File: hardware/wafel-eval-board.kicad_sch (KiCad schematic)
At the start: 57 parts, among them Q101 AO3422, U101 TPS70933, U102 LM5163DDA

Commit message: fixes
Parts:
- removed H101: BAT+, MountingHole:MountingHole_3.2mm_M3_Pad, symbol Mechanical:MountingHole_Pad
- removed H102: CELL15, MountingHole:MountingHole_3.2mm_M3_Pad, symbol Mechanical:MountingHole_Pad
- removed H103: CELL13, MountingHole:MountingHole_3.2mm_M3_Pad, symbol Mechanical:MountingHole_Pad
- removed H104: CELL11, MountingHole:MountingHole_3.2mm_M3_Pad, symbol Mechanical:MountingHole_Pad
- removed H111: CELL16, MountingHole:MountingHole_3.2mm_M3_Pad, symbol Mechanical:MountingHole_Pad
- removed H112: CELL14, MountingHole:MountingHole_3.2mm_M3_Pad, symbol Mechanical:MountingHole_Pad
- removed H113: CELL12, MountingHole:MountingHole_3.2mm_M3_Pad, symbol Mechanical:MountingHole_Pad
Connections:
- net CELL10: now also F101.1, F102.1
- removed net CELL17: F101.1, F102.1, F103.2
- new net CELL_TOP: F103.2
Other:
- added sheet CB Mosfets (cb-mosfets.kicad_sch)
- sheet Frontend ports: added VC[0..10]; removed CELL[0..17], CH
- sheet MCU ports: added BAT{ADC EN}; removed none
- moved on the sheet: F101, F102, H105, H106, H107, H108, H109, H110, H114, H115, H116, H117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

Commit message: add bat{en adc}
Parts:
- renumbered H105 to H101, H106 to H102, H107 to H103, H108 to H104, H109 to H105, H110 to H106, H114 to H107, H115 to H108, H116 to H109, H117 to H110, H118 to H111, H119 to H112, H120 to H113, H121 to H114
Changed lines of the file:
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@@
 		(in_pos_files yes)
 		(dnp no)
-		(property "Reference" "H109"
+		(property "Reference" "H105"
 			(at 29.21 130.8099 90)
 			(show_name no)
@@
 			(project "wafel-eval-board"
 				(path "/3e668e3e-3e16-4665-a807-4735962c41d3"
-					(reference "H109")
+					(reference "H105")
 					(unit 1)
 				)
@@
 		(in_pos_files yes)
 		(dnp no)
-		(property "Reference" "H116"
+		(property "Reference" "H109"
 			(at 43.18 118.1099 90)
 			(show_name no)
@@
 			(project "wafel-eval-board"
 				(path "/3e668e3e-3e16-4665-a807-4735962c41d3"
-					(reference "H116")
+					(reference "H109")
 					(unit 1)
 				)
@@
 		(in_pos_files yes)
 		(dnp no)
-		(property "Reference" "H106"
+		(property "Reference" "H102"
 			(at 29.21 115.5699 90)
 			(show_name no)
@@
 			(project "wafel-eval-board"
 				(path "/3e668e3e-3e16-4665-a807-4735962c41d3"
-					(reference "H106")
+					(reference "H102")
 					(unit 1)
 				)
@@
 		(in_pos_files yes)
 		(dnp no)
-		(property "Reference" "H115"
+		(property "Reference" "H108"
 			(at 43.18 113.0299 90)
 			(show_name no)
@@
 			(project "wafel-eval-board"
 				(path "/3e668e3e-3e16-4665-a807-4735962c41d3"
-					(reference "H115")
+					(reference "H108")
 					(unit 1)
 				)
@@
 		(in_pos_files yes)
 		(dnp no)
-		(property "Reference" "H108"
+		(property "Reference" "H104"
 			(at 29.21 125.7299 90)
 			(show_name no)
@@
 			(project "wafel-eval-board"
 				(path "/3e668e3e-3e16-4665-a807-4735962c41d3"
-					(reference "H108")
+					(reference "H104")
 					(unit 1)
 				)
@@
 		(in_pos_files yes)
 		(dnp no)
-		(property "Reference" "H105"
+		(property "Reference" "H101"
 			(at 29.21 110.4899 90)
 			(show_name no)
@@
 			(project "wafel-eval-board"
 				(path "/3e668e3e-3e16-4665-a807-4735962c41d3"
-					(reference "H105")
+					(reference "H101")
 					(unit 1)
 				)
@@
 		(in_pos_files yes)
 		(dnp no)
-		(property "Reference" "H120"
+		(property "Reference" "H113"
 			(at 273.05 146.0499 90)
 			(show_name no)
@@
 			(project "wafel-eval-board"
 				(path "/3e668e3e-3e16-4665-a807-4735962c41d3"
-					(reference "H120")
+					(reference "H113")
 					(unit 1)
 				)
@@
 		(in_pos_files yes)
 		(dnp no)
-		(property "Reference" "H121"
+		(property "Reference" "H114"
 			(at 273.05 153.6699 90)
 			(show_name no)
@@
 			(project "wafel-eval-board"
 				(path "/3e668e3e-3e16-4665-a807-4735962c41d3"
-					(reference "H121")
+					(reference "H114")
 					(unit 1)
 				)
@@
 		(in_pos_files yes)
 		(dnp no)
-		(property "Reference" "H110"
+		(property "Reference" "H106"
 			(at 24.13 135.89 90)
 			(show_name no)
@@
 			(project "wafel-eval-board"
 				(path "/3e668e3e-3e16-4665-a807-4735962c41d3"
-					(reference "H110")
+					(reference "H106")
 					(unit 1)
 				)
@@
 		(in_pos_files yes)
 		(dnp no)
-		(property "Reference" "H119"
+		(property "Reference" "H112"
 			(at 43.18 133.3499 90)
 			(show_name no)
@@
 			(project "wafel-eval-board"
 				(path "/3e668e3e-3e16-4665-a807-4735962c41d3"
-					(reference "H119")
+					(reference "H112")
 					(unit 1)
 				)
@@
 		(in_pos_files yes)
 		(dnp no)
-		(property "Reference" "H117"
+		(property "Reference" "H110"
 			(at 43.18 123.1899 90)
 			(show_name no)
@@
 			(project "wafel-eval-board"
 				(path "/3e668e3e-3e16-4665-a807-4735962c41d3"
-					(reference "H117")
+					(reference "H110")
 					(unit 1)
 				)
@@
 		(in_pos_files yes)
 		(dnp no)
-		(property "Reference" "H118"
+		(property "Reference" "H111"
 			(at 43.18 128.2699 90)
 			(show_name no)
@@
 			(project "wafel-eval-board"
 				(path "/3e668e3e-3e16-4665-a807-4735962c41d3"
-					(reference "H118")
+					(reference "H111")
 					(unit 1)
 				)
@@
 		(in_pos_files yes)
 		(dnp no)
-		(property "Reference" "H107"
+		(property "Reference" "H103"
 			(at 29.21 120.6499 90)
 			(show_name no)
@@
 			(project "wafel-eval-board"
 				(path "/3e668e3e-3e16-4665-a807-4735962c41d3"
-					(reference "H107")
+					(reference "H103")
 					(unit 1)
 				)
@@
 		(in_pos_files yes)
 		(dnp no)
-		(property "Reference" "H114"
+		(property "Reference" "H107"
 			(at 43.18 107.9499 90)
 			(show_name no)
@@
 			(project "wafel-eval-board"
 				(path "/3e668e3e-3e16-4665-a807-4735962c41d3"
-					(reference "H114")
+					(reference "H107")
 					(unit 1)
 				)

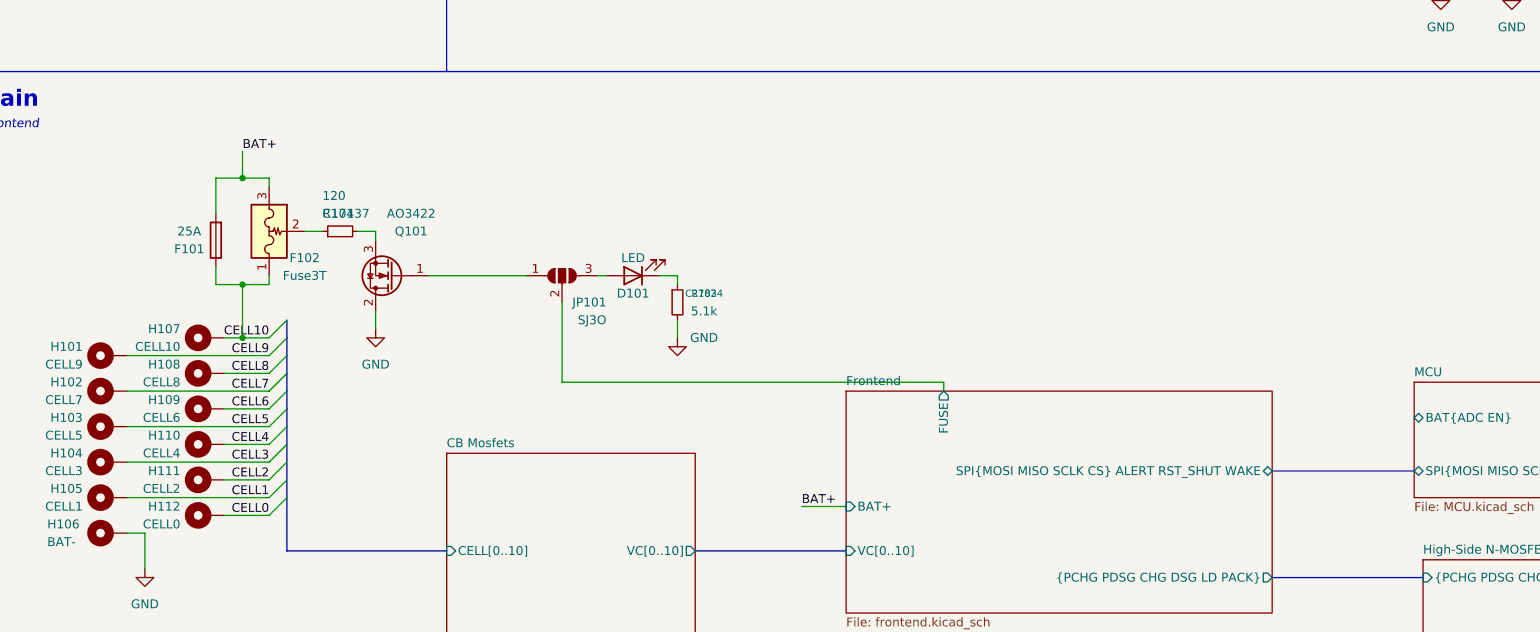
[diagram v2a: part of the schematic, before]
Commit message: simplify page
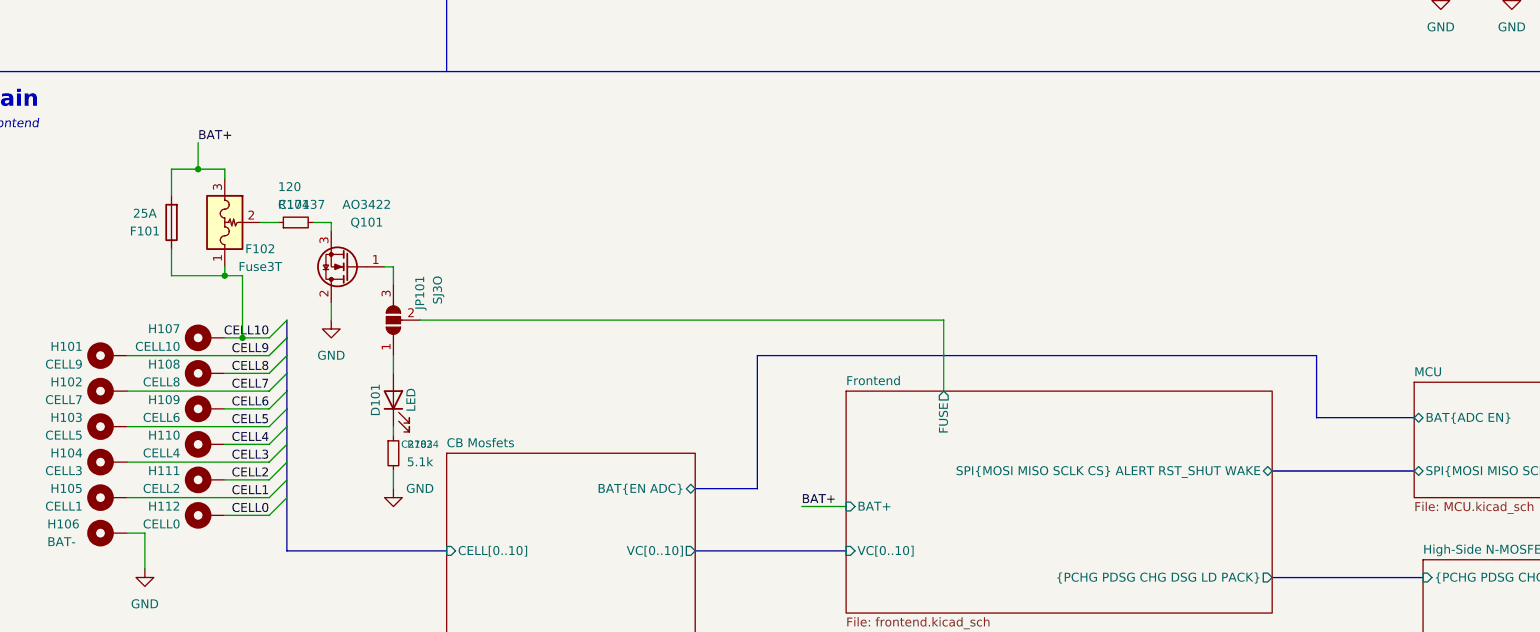
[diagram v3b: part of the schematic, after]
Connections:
- net at D101.2 (A): now also JP101.1 (A); no longer JP101.3 (B)
- net at Q101.1 (G): now also JP101.3 (B); no longer JP101.1 (A)
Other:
- sheet CB Mosfets ports: added BAT{EN ADC}; removed none
- moved on the sheet: D101, F101, F102, JP101, Q101, R101, R102

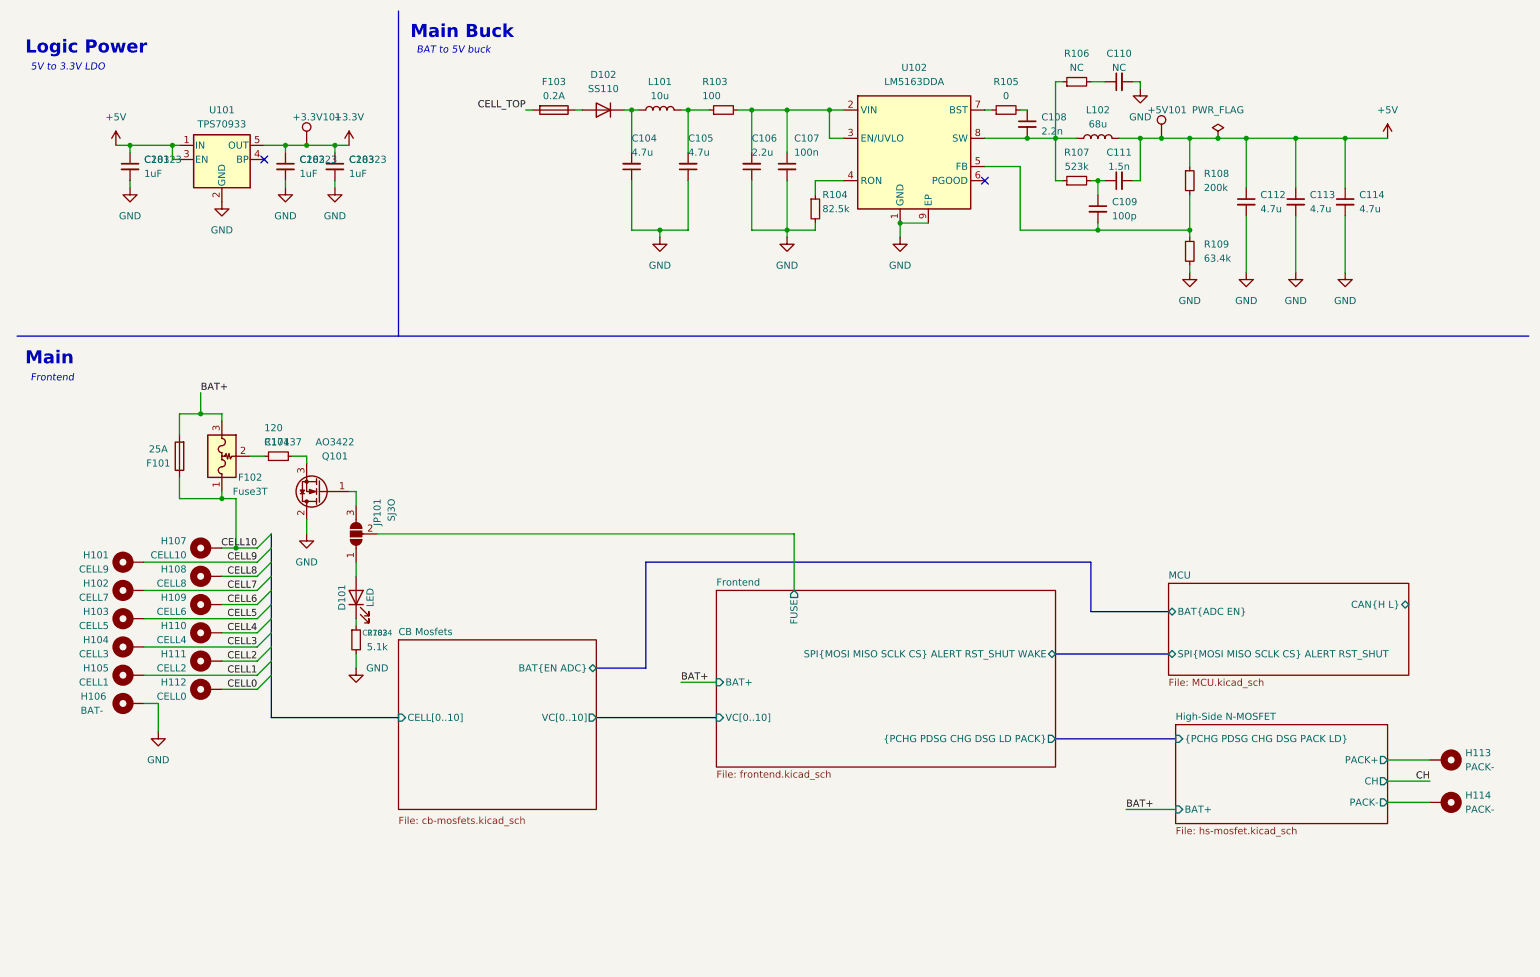
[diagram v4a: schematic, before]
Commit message: switch capasitors to 220mf
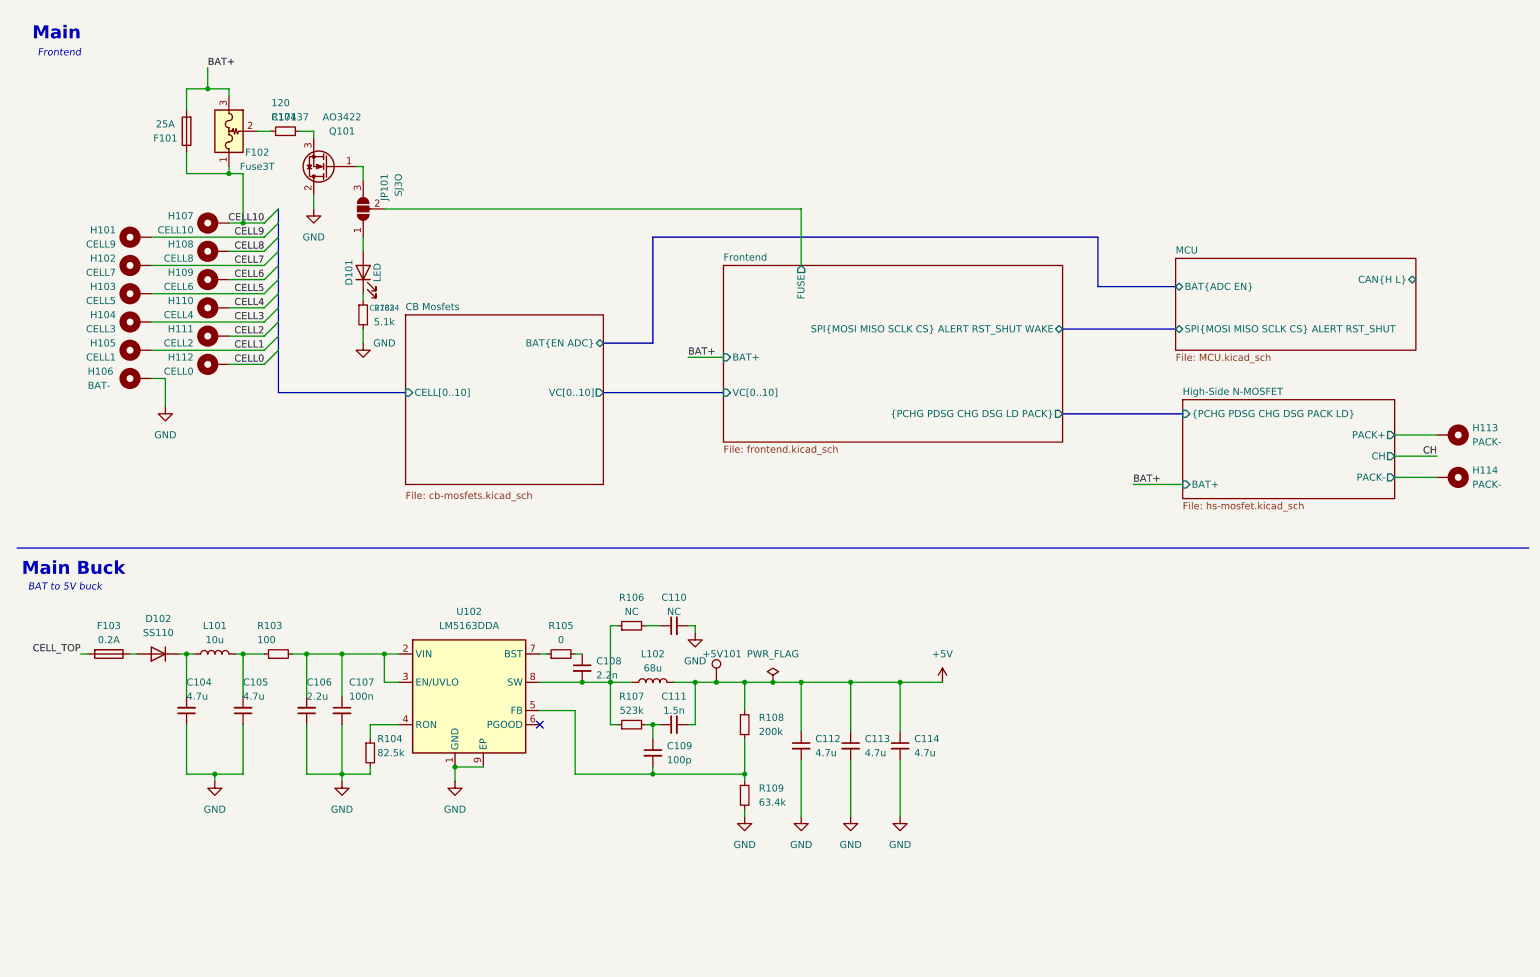
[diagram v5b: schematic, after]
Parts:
- removed +3.3V101: TestPoint, TestPoint:TestPoint_Pad_D1.0mm, symbol Connector:TestPoint
- removed C101, C102, C103: 1uF, Capacitor_SMD:C_0805_2012Metric, symbol Device:C_Small
- removed U101: TPS70933, Package_TO_SOT_SMD:SOT-23-5, symbol Regulator_Linear:TPS79333-EP
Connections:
- no-connect marks 2 -> 1
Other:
- note removed: "5V to 3.3V LDO"
- note removed: "Logic Power"
- moved on the sheet: +5V101, C104, C105, C106, C107, C108, C109, C110, C111, C112, C113, C114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

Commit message: x
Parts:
- removed D101: LED, LED_THT:LED_D3.0mm, symbol Device:LED
- removed F101: 25A, Fuse:Fuse_Littelfuse-NANO2-451_453, symbol Device:Fuse
- removed F102: Fuse3T, symbol wafel-eval-board:Fuse_3Terminal
- removed R101: 120, Resistor_SMD:R_0805_2012Metric, symbol Device:R_Small
- added D102: LED, LED_THT:LED_D3.0mm, symbol Device:LED
- added F102: 25A, Fuse:Fuse_Littelfuse-NANO2-451_453, symbol Device:Fuse
- added F103: Fuse3T, symbol wafel-eval-board:Fuse_3Terminal
- added R103: 5.1k, Resistor_SMD:R_0805_2012Metric, symbol Device:R_Small
- C109: renamed from C112; footprint Capacitor_SMD:C_0805_2012Metric -> Capacitor_SMD:C_1206_3216Metric; LCSC (none) -> C577211
- C110: renamed from C113; footprint Capacitor_SMD:C_0805_2012Metric -> Capacitor_SMD:C_1206_3216Metric; LCSC (none) -> C577211
- C111: renamed from C114; footprint Capacitor_SMD:C_0805_2012Metric -> Capacitor_SMD:C_1206_3216Metric; LCSC (none) -> C577211
- R102: value 5.1k -> 120; LCSC C27834 -> C17437
- R104: value 82.5k -> 82.5K
- R107: value 523k -> 523K
- R108: value 200k -> 200K
- renumbered C104 to C101, C105 to C102, C106 to C103, C107 to C104, C108 to C105, C109 to C106, C110 to C107, C111 to C108, D102 to D101, F103 to F101, R103 to R101, U102 to U101
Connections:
- net CELL_TOP is gone; now on net CELL10: F101.2
- net BAT+: now also F102.2, F103.3
- net CELL10: now also F102.1, F103.1
- net GND: now also R103.2; no longer R102.2
- net at R102.1: now also F103.2
- net at JP101.1 (A): now also Q101.1 (G)
- net at Q101.3 (S): now also R102.2
- net at JP101.3 (B): now also D102.2 (A); no longer Q101.1 (G)
- net Frontend/FUSE renamed FUSE
- new net: D102.1 (K), R103.1
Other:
- note added: "Fuse"

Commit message: x
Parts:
- R106: value NC -> 0
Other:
- moved on the sheet: +5V101
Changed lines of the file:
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@@
 	)
 	(junction
-		(at 138.43 133.35)
-		(diameter 0)
-		(color 0 0 0 0)
-	)
-	(junction
 		(at 91.44 148.59)
 		(diameter 0)
@@
 	(wire
 		(pts
-			(xy 138.43 133.35) (xy 143.51 133.35)
-		)
-		(stroke
-			(width 0)
-			(type default)
-		)
-	)
-	(wire
-		(pts
 			(xy 212.09 139.7) (xy 212.09 135.89)
 		)
@@
 	(wire
 		(pts
-			(xy 134.62 133.35) (xy 138.43 133.35)
+			(xy 134.62 133.35) (xy 143.51 133.35)
 		)
 		(stroke
@@
 			)
 		)
-		(property "Value" "NC"
+		(property "Value" "0"
 			(at 123.19 120.65 90)
 			(show_name no)
@@
 	(symbol
 		(lib_id "Connector:TestPoint")
-		(at 138.43 133.35 0)
+		(at 162.56 133.35 0)
 		(unit 1)
 		(body_style 1)
@@
 		(dnp no)
 		(property "Reference" "+5V101"
-			(at 135.89 128.27 0)
+			(at 160.02 128.27 0)
 			(show_name no)
 			(do_not_autoplace no)
@@
 		)
 		(property "Value" "TestPoint"
-			(at 140.97 131.3179 0)
+			(at 165.1 131.3179 0)
 			(hide yes)
 			(show_name no)
@@
 		)
 		(property "Footprint" "TestPoint:TestPoint_Pad_D1.0mm"
-			(at 143.51 133.35 0)
+			(at 167.64 133.35 0)
 			(hide yes)
 			(show_name no)
@@
 		)
 		(property "Datasheet" ""
-			(at 143.51 133.35 0)
+			(at 167.64 133.35 0)
 			(hide yes)
 			(show_name no)
@@
 		)
 		(property "Description" "test point"
-			(at 138.43 133.35 0)
+			(at 162.56 133.35 0)
 			(hide yes)
 			(show_name no)

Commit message: x
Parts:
- added H115: PACK-, MountingHole:MountingHole_3.2mm_M3_Pad, symbol Mechanical:MountingHole_Pad
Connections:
- net CH: now also H115.1
- net GND: now also Q101.3 (S), R103.1; no longer Q101.2 (D), R103.2
- net at R102.2: now also Q101.2 (D); no longer Q101.3 (S)
- net at D102.1 (K): now also R103.2; no longer R103.1
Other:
- sheet MCU ports: added VESC{SW GND}; removed none
- moved on the sheet: D102, F102, F103, H113, H114, JP101, Q101, R102, R103
